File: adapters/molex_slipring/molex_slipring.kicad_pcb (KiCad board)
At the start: 4 copper layers, 66 x 40 mm, 7 parts, among them J1 RJ45 RJE591885401, J2 5055680571

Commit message: Verify JLC stack impedance, update PCB widths, and document ordering options with screenshots
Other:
- board text added: "A-DRAFT / VERIFY MATE + CAM"
- board text removed: "A-DRAFT / VERIFY MATE + IMPEDANCE"
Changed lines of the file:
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@@
 		(rev "A-DRAFT")
 		(comment 1 "MOLEX 5P / SLIPRING; PIN 5 NC; VERIFY HOUSING")
-		(comment 2 "JLC04161H-7628 / 100R trunk W0.23 G0.22 / verify manufacturer mating")
+		(comment 2 "JLC04161H-7628 / 100R trunk W0.234 G0.216 / verify manufacturer mating")
 	)
 	(layers
@@
 		(layer "Edge.Cuts")
 	)
-	(gr_text "A-DRAFT / VERIFY MATE + IMPEDANCE"
+	(gr_text "A-DRAFT / VERIFY MATE + CAM"
 		(at 33 37 0)
 		(layer "F.SilkS")
@@
 		(start 22 16.39)
 		(end 26 16.945)
-		(width 0.23)
+		(width 0.234)
 		(layer "F.Cu")
 		(net "/PAIR_A_P")
@@
 		(start 26 16.945)
 		(end 30 17.5)
-		(width 0.23)
+		(width 0.234)
 		(layer "F.Cu")
 		(net "/PAIR_A_P")
@@
 		(start 30 17.5)
 		(end 42 17.5)
-		(width 0.23)
+		(width 0.234)
 		(layer "F.Cu")
 		(net "/PAIR_A_P")
@@
 		(start 42 17.5)
 		(end 44 17.5)
-		(width 0.23)
+		(width 0.234)
 		(layer "F.Cu")
 		(net "/PAIR_A_P")
@@
 		(start 44 17.5)
 		(end 46.81 17.5)
-		(width 0.23)
+		(width 0.234)
 		(layer "F.Cu")
 		(net "/PAIR_A_P")
@@
 		(start 26 20.632319)
 		(end 30 17.95)
-		(width 0.23)
+		(width 0.234)
 		(layer "F.Cu")
 		(net "/PAIR_A_N")
@@
 		(start 22 17.41)
 		(end 26 20.632319)
-		(width 0.23)
+		(width 0.234)
 		(layer "F.Cu")
 		(net "/PAIR_A_N")
@@
 		(start 42 17.95)
 		(end 44 18.75)
-		(width 0.23)
+		(width 0.234)
 		(layer "F.Cu")
 		(net "/PAIR_A_N")
@@
 		(start 44 18.75)
 		(end 46.81 18.75)
-		(width 0.23)
+		(width 0.234)
 		(layer "F.Cu")
 		(net "/PAIR_A_N")
@@
 		(start 30 17.95)
 		(end 42 17.95)
-		(width 0.23)
+		(width 0.234)
 		(layer "F.Cu")
 		(net "/PAIR_A_N")
@@
 		(start 44 20)
 		(end 46.81 20)
-		(width 0.23)
+		(width 0.234)
 		(layer "F.Cu")
 		(net "/PAIR_B_P")
@@
 		(start 30 20)
 		(end 42 20)
-		(width 0.23)
+		(width 0.234)
 		(layer "B.Cu")
 		(net "/PAIR_B_P")
@@
 		(start 26 19.215)
 		(end 30 20)
-		(width 0.23)
+		(width 0.234)
 		(layer "B.Cu")
 		(net "/PAIR_B_P")
@@
 		(start 22 18.43)
 		(end 26 19.215)
-		(width 0.23)
+		(width 0.234)
 		(layer "B.Cu")
 		(net "/PAIR_B_P")
@@
 		(start 42 20)
 		(end 44 20)
-		(width 0.23)
+		(width 0.234)
 		(layer "B.Cu")
 		(net "/PAIR_B_P")
@@
 		(start 44 21.25)
 		(end 46.81 21.25)
-		(width 0.23)
+		(width 0.234)
 		(layer "F.Cu")
 		(net "/PAIR_B_N")
@@
 		(start 30 20.45)
 		(end 42 20.45)
-		(width 0.23)
+		(width 0.234)
 		(layer "B.Cu")
 		(net "/PAIR_B_N")
@@
 		(start 42 20.45)
 		(end 44 21.25)
-		(width 0.23)
+		(width 0.234)
 		(layer "B.Cu")
 		(net "/PAIR_B_N")
@@
 		(start 22 21.49)
 		(end 26 23.964817)
-		(width 0.23)
+		(width 0.234)
 		(layer "B.Cu")
 		(net "/PAIR_B_N")
@@
 		(start 26 23.964817)
 		(end 30 20.45)
-		(width 0.23)
+		(width 0.234)
 		(layer "B.Cu")
 		(net "/PAIR_B_N")

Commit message: Refine Molex slip-ring adapter routing
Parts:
- removed TP1: Shield_SolderPoint, adapter:Shield_SolderPoint
- moved J2 1.32 mm to (48.2, 18.7)
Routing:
- net /PAIR_B_P: track 30.0 -> 31.8 mm, vias 1 -> 0
- net /PAIR_A_P: track 29.9 -> 30.7 mm
- net /PAIR_A_N: track 29.9 -> 29.3 mm
- net /PAIR_B_N: vias 1 -> 0
- net /SHIELD: vias 12 -> 8

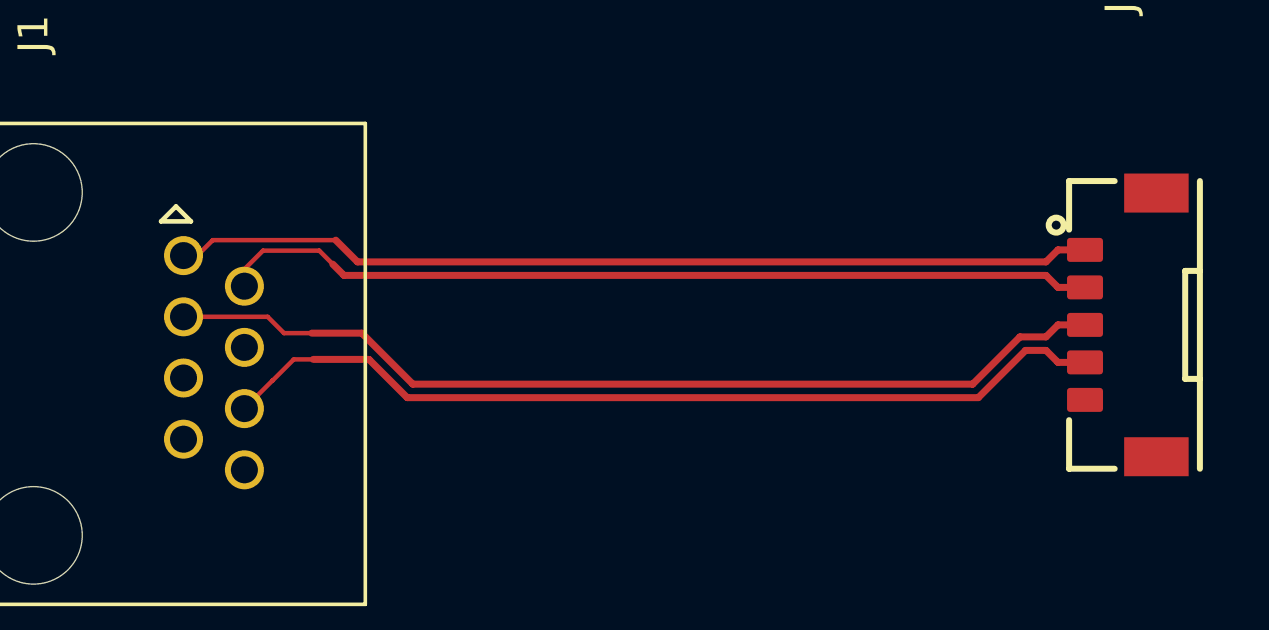
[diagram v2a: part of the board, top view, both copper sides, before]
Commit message: Refine Molex pair escapes and reduce skew without signal vias
Keep the latest all-F.Cu layout and connector placement, use 0.234 mm signal traces throughout, and reduce PCB pair skew to 0.792/0.987 mm. Extend uniform coupled trunks while documenting inter-pair spacing tradeoffs.

Preserve the concurrent M12 routing and shared constraint updates. Retain the new gap/skew/uncoupled/via DRC checks, remove only the Molex narrow-trace exception, and support per-board verification.

KiCad 10.0.6 DRC/ERC/parity, exact pinmap, NC isolation, netclass settings and generator geometry checks passed. Include before/after evidence and clarify the scope of the 1.27 mm PHY guideline.
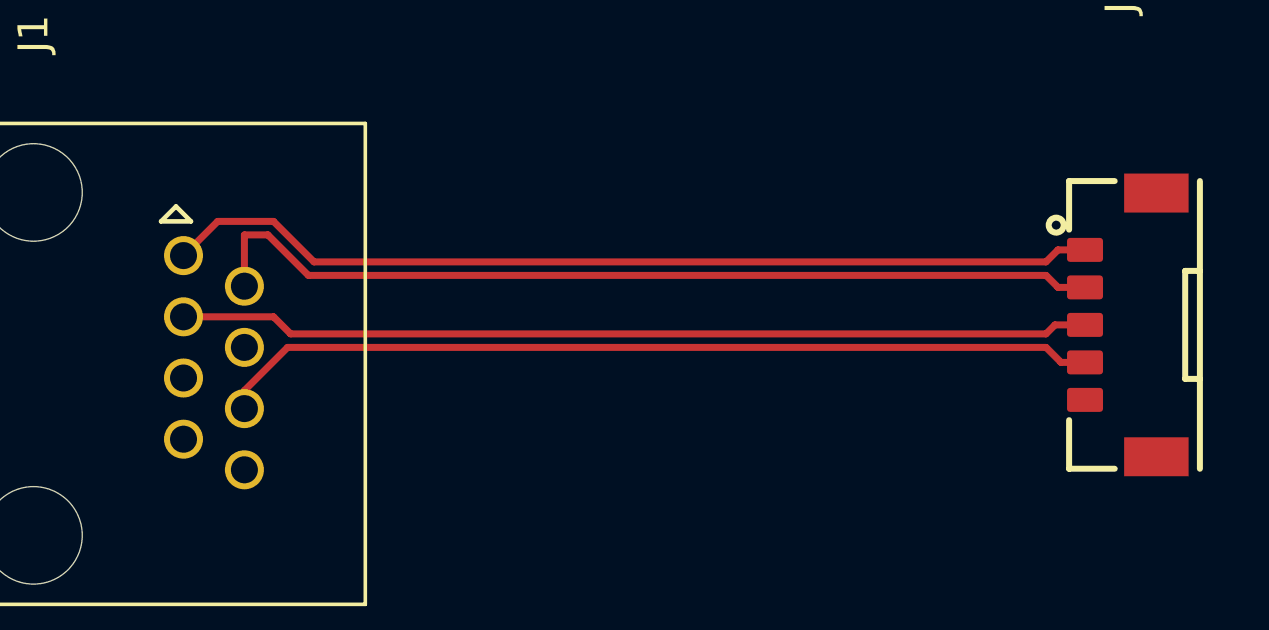
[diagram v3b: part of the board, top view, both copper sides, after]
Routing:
- net /PAIR_B_P: track 31.8 -> 30.4 mm
- net /PAIR_A_N: track 29.3 -> 30.5 mm
- net /PAIR_B_N: track 30.0 -> 29.4 mm
- net /PAIR_A_P: track 30.7 -> 31.2 mm
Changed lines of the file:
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@@
 	)
 	(segment
-		(start 17.01 16.4)
-		(end 17.45 16.4)
-		(width 0.15)
-		(layer "F.Cu")
-		(net "/PAIR_A_P")
-	)
-	(segment
-		(start 45.749999 16.6)
-		(end 22.8 16.6)
+		(start 46.15 16.2)
+		(end 47.05 16.2)
 		(width 0.234)
 		(layer "F.Cu")
@@
 	)
 	(segment
-		(start 47.05 16.2)
-		(end 46.149999 16.2)
+		(start 45.75 16.6)
+		(end 46.15 16.2)
 		(width 0.234)
 		(layer "F.Cu")
@@
 	)
 	(segment
-		(start 46.149999 16.2)
-		(end 45.749999 16.6)
+		(start 21.35 16.6)
+		(end 45.75 16.6)
+		(width 0.234)
+		(layer "F.Cu")
+		(net "/PAIR_A_P")
+	)
+	(segment
+		(start 20 15.25)
+		(end 21.35 16.6)
 		(width 0.234)
 		(layer "F.Cu")
@@
 	(segment
 		(start 17 16.39)
-		(end 17.01 16.4)
-		(width 0.15)
-		(layer "F.Cu")
-		(net "/PAIR_A_P")
-	)
-	(segment
-		(start 22.8 16.6)
-		(end 22.075 15.875)
+		(end 18.14 15.25)
 		(width 0.234)
 		(layer "F.Cu")
@@
 	)
 	(segment
-		(start 17.45 16.4)
-		(end 17.975 15.875)
-		(width 0.15)
+		(start 18.14 15.25)
+		(end 20 15.25)
+		(width 0.234)
 		(layer "F.Cu")
 		(net "/PAIR_A_P")
 	)
 	(segment
-		(start 17.975 15.875)
-		(end 22.075 15.875)
-		(width 0.15)
-		(layer "F.Cu")
-		(net "/PAIR_A_P")
-	)
-	(segment
-		(start 45.749999 17.05)
-		(end 22.35 17.05)
+		(start 45.75 17.05)
+		(end 46.15 17.45)
 		(width 0.234)
 		(layer "F.Cu")
@@
 	)
 	(segment
-		(start 19.03 16.845)
-		(end 19.65 16.225)
-		(width 0.15)
-		(layer "F.Cu")
-		(net "/PAIR_A_N")
-	)
-	(segment
-		(start 22.35 17.05)
-		(end 21.975 16.675)
+		(start 19.03 15.7)
+		(end 19.813604 15.7)
 		(width 0.234)
 		(layer "F.Cu")
@@
 	)
 	(segment
-		(start 47.05 17.45)
-		(end 46.149999 17.45)
+		(start 21.163604 17.05)
+		(end 45.75 17.05)
 		(width 0.234)
 		(layer "F.Cu")
@@
 	)
 	(segment
-		(start 19.65 16.225)
-		(end 21.525 16.225)
-		(width 0.15)
-		(layer "F.Cu")
-		(net "/PAIR_A_N")
-	)
-	(segment
 		(start 19.03 17.41)
-		(end 19.03 16.845)
-		(width 0.15)
-		(layer "F.Cu")
-		(net "/PAIR_A_N")
-	)
-	(segment
-		(start 21.525 16.225)
-		(end 21.975 16.675)
-		(width 0.15)
-		(layer "F.Cu")
-		(net "/PAIR_A_N")
-	)
-	(segment
-		(start 46.149999 17.45)
-		(end 45.749999 17.05)
+		(end 19.03 15.7)
 		(width 0.234)
 		(layer "F.Cu")
@@
 	)
 	(segment
-		(start 44.881802 19.1)
-		(end 43.306802 20.675)
+		(start 46.15 17.45)
+		(end 47.05 17.45)
+		(width 0.234)
+		(layer "F.Cu")
+		(net "/PAIR_A_N")
+	)
+	(segment
+		(start 19.813604 15.7)
+		(end 21.163604 17.05)
+		(width 0.234)
+		(layer "F.Cu")
+		(net "/PAIR_A_N")
+	)
+	(segment
+		(start 45.75 19)
+		(end 46.05 18.7)
 		(width 0.234)
 		(layer "F.Cu")
@@
 	)
 	(segment
-		(start 47.05 18.7)
-		(end 46.149999 18.7)
+		(start 17 18.43)
+		(end 20 18.43)
 		(width 0.234)
 		(layer "F.Cu")
@@
 	)
 	(segment
-		(start 24.643198 20.675)
-		(end 22.943198 18.975)
+		(start 46.05 18.7)
+		(end 47.05 18.7)
 		(width 0.234)
 		(layer "F.Cu")
@@
 	)
 	(segment
-		(start 22.943198 18.975)
-		(end 21.275 18.975)
+		(start 20 18.43)
+		(end 20.57 19)
 		(width 0.234)
 		(layer "F.Cu")
@@
 	)
 	(segment
-		(start 45.749999 19.1)
-		(end 44.881802 19.1)
+		(start 20.57 19)
+		(end 45.75 19)
 		(width 0.234)
 		(layer "F.Cu")
@@
 	)
 	(segment
-		(start 19.805 18.43)
-		(end 20.35 18.975)
-		(width 0.15)
-		(layer "F.Cu")
-		(net "/PAIR_B_P")
-	)
-	(segment
-		(start 17 18.43)
-		(end 19.805 18.43)
-		(width 0.15)
-		(layer "F.Cu")
-		(net "/PAIR_B_P")
-	)
-	(segment
-		(start 46.149999 18.7)
-		(end 45.749999 19.1)
-		(width 0.234)
-		(layer "F.Cu")
-		(net "/PAIR_B_P")
-	)
-	(segment
-		(start 43.306802 20.675)
-		(end 24.643198 20.675)
-		(width 0.234)
-		(layer "F.Cu")
-		(net "/PAIR_B_P")
-	)
-	(segment
-		(start 20.35 18.975)
-		(end 21.275 18.975)
-		(width 0.15)
-		(layer "F.Cu")
-		(net "/PAIR_B_P")
-	)
-	(segment
-		(start 45.068198 19.55)
-		(end 43.493198 21.125)
+		(start 19.03 20.89)
+		(end 20.47 19.45)
 		(width 0.234)
 		(layer "F.Cu")
@@
 	)
 	(segment
-		(start 19.97 20.55)
-		(end 19.975 20.55)
-		(width 0.15)
-		(layer "F.Cu")
-		(net "/PAIR_B_N")
-	)
-	(segment
-		(start 46.149999 19.95)
-		(end 45.749999 19.55)
+		(start 20.47 19.45)
+		(end 45.75 19.45)
 		(width 0.234)
 		(layer "F.Cu")
@@
 	)
 	(segment
-		(start 23.181802 19.85)
-		(end 21.325 19.85)
+		(start 46.25 19.95)
+		(end 47.05 19.95)
 		(width 0.234)
 		(layer "F.Cu")
@@
 	)
 	(segment
-		(start 47.05 19.95)
-		(end 46.149999 19.95)
+		(start 19.03 21.49)
+		(end 19.03 20.89)
 		(width 0.234)
 		(layer "F.Cu")
@@
 	)
 	(segment
-		(start 20.675 19.85)
-		(end 21.325 19.85)
-		(width 0.15)
-		(layer "F.Cu")
-		(net "/PAIR_B_N")
-	)
-	(segment
-		(start 45.749999 19.55)
-		(end 45.068198 19.55)
+		(start 45.75 19.45)
+		(end 46.25 19.95)
 		(width 0.234)
 		(layer "F.Cu")
-		(net "/PAIR_B_N")
-	)
-	(segment
-		(start 19.975 20.55)
-		(end 20.675 19.85)
-		(width 0.15)
-		(layer "F.Cu")
-		(net "/PAIR_B_N")
-	)
-	(segment
-		(start 19.03 21.49)
-		(end 19.97 20.55)
-		(width 0.15)
-		(layer "F.Cu")
-		(net "/PAIR_B_N")
-	)
-	(segment
-		(start 24.456802 21.125)
-		(end 23.181802 19.85)
-		(width 0.234)
-		(layer "F.Cu")
-		(net "/PAIR_B_N")
-	)
-	(segment
-		(start 43.493198 21.125)
-		(end 24.456802 21.125)
-		(width 0.234)
-		(layer "F.Cu")
